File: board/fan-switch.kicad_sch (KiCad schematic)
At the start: 23 parts, among them J1 Conn_01x01, Q1 BXT420N03M, U1 LM1117-3.3

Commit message: WIP
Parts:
- removed ?: (no value), symbol Device:D_Schottky_Dual_CommonCathode_AAK_Parallel
- removed ?: (no value), symbol Drake:ESP-PROG
- removed ? (x5): (no value), symbol Device:R
- removed ? (x4): (no value), symbol Device:C
- removed ?: (no value), symbol Drake:ESP-12
- removed C5: 10u, symbol Device:C_Polarized
- removed C6: 10uF, symbol Device:C_Polarized
- added C1: 10u, Capacitor_SMD:C_0805_2012Metric_Pad1.18x1.45mm_HandSolder, symbol Device:C
- added C2, C3: 47u, Capacitor_SMD:C_0805_2012Metric_Pad1.18x1.45mm_HandSolder, symbol Device:C
- added D1: LED, LED_SMD:LED_0805_2012Metric_Pad1.15x1.40mm_HandSolder, symbol Device:LED
- added J2: PROG, Connector_PinHeader_2.54mm:PinHeader_1x03_P2.54mm_Vertical, symbol Connector:Conn_01x03_Female
- added R1: 270R, Resistor_SMD:R_0805_2012Metric_Pad1.20x1.40mm_HandSolder, symbol Device:R
- added U2: ESP32-C3-WROOM-02, Espressif:ESP32-C3-WROOM-02, symbol Espressif:ESP32-C3-WROOM-02
- D1: renamed from U; value (none) -> SK22; footprint (none) -> Diode_SMD:D_SMB_Handsoldering
- J1: value Conn_01x01 -> 12V; footprint (none) -> Connector_Wire:SolderWire-1sqmm_1x01_D1.4mm_OD3.9mm
- J2: renamed from J1; value Conn_01x01 -> GND; footprint (none) -> Connector_Wire:SolderWire-1sqmm_1x01_D1.4mm_OD3.9mm
- J3: renamed from J1; value Conn_01x01 -> M+; footprint (none) -> Connector_Wire:SolderWire-1sqmm_1x01_D1.4mm_OD3.9mm
- J4: renamed from J1; value Conn_01x01 -> M-; footprint (none) -> Connector_Wire:SolderWire-1sqmm_1x01_D1.4mm_OD3.9mm
- Q1: footprint Package_TO_SOT_SMD:SOT-23_Handsoldering -> Package_TO_SOT_SMD:SOT-23
- R1: renamed from ?; value (none) -> 100; footprint (none) -> Resistor_SMD:R_0805_2012Metric_Pad1.20x1.40mm_HandSolder
- R2: renamed from ?; value (none) -> 10k; footprint (none) -> Resistor_SMD:R_0805_2012Metric_Pad1.20x1.40mm_HandSolder
- U1: footprint (none) -> Package_TO_SOT_SMD:SOT-223-3_TabPin2
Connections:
- net +12V: now also C1.1
- net GATE: now also U2.15 (GPIO3/ADC1_CH3)
- net GND: now also C1.2, C2.2, C3.2, D1.1 (K), J2.2 (Pin_2), U2.19 (GND), U2.9 (GND)
- net 3V3-LOCAL renamed +3V3
- net +3V3: now also C2.1, C3.1, U2.1 (3V3), U2.2 (EN/CHIP_PU)
- new net: D1.2 (A), R1.2
- new net LED: R1.1, U2.3 (GPIO4/ADC1_CH4)
- new net USB_D+: J2.1 (Pin_1), U2.14 (GPIO19/USB_D+)
- new net USB_D-: J2.3 (Pin_3), U2.13 (GPIO18/USB_D-)
- no-connect marks 6 -> 11
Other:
- moved on the sheet: D1, J1, J2, J3, J4, Q1

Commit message: 2.1
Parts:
- removed J2: PROG, Connector_PinHeader_2.54mm:PinHeader_1x03_P2.54mm_Vertical, symbol Connector:Conn_01x03_Female
- removed U1: LM1117-3.3, Package_TO_SOT_SMD:SOT-223-3_TabPin2, symbol Regulator_Linear:LM1117-3.3
- removed U2: ESP32-C3-WROOM-02, Espressif:ESP32-C3-WROOM-02, symbol Espressif:ESP32-C3-WROOM-02
- added A1: 31mm, Drake:Wire antena 2.4GHz, symbol Device:Antenna
- added C4: 10u, Capacitor_SMD:C_0805_2012Metric, symbol Device:C
- added C5, C6: 100n, Capacitor_SMD:C_0805_2012Metric, symbol Device:C
- added J3: TX, Connector_PinHeader_2.54mm:PinHeader_1x01_P2.54mm_Vertical, symbol Connector_Generic:Conn_01x01
- added U1: LM1117MP-3.3, Package_TO_SOT_SMD:SOT-223-3_TabPin2, symbol Regulator_Linear:LM1117MP-3.3
- added U2: PAN2110P0AA, Package_SO:SOIC-8_3.9x4.9mm_P1.27mm, symbol Drake:PAN2110P0AA
- added U3: PY32F003W1xSx, Package_SO:SOIC-16_3.9x9.9mm_P1.27mm, symbol MCU_Puya_PY32F:PY32F003W1xSx
- added X1: SWD, Drake:SWD, symbol Drake:SWD
- added Y1: 16MHz, Crystal:Crystal_SMD_3225-4Pin_3.2x2.5mm, symbol Device:Crystal_GND24_Small
- C1: footprint Capacitor_SMD:C_0805_2012Metric_Pad1.18x1.45mm_HandSolder -> Capacitor_SMD:C_0805_2012Metric
- C2: value 47u -> 1u; footprint Capacitor_SMD:C_0805_2012Metric_Pad1.18x1.45mm_HandSolder -> Capacitor_SMD:C_0805_2012Metric
- C3: value 47u -> 100n; footprint Capacitor_SMD:C_0805_2012Metric_Pad1.18x1.45mm_HandSolder -> Capacitor_SMD:C_0805_2012Metric
- Q1: value BXT420N03M -> AO3400A
- R3: renamed from R1; value 270R -> 330R
- renumbered D1 to D2, J3 to J4, J4 to J5, R2 to R1, R1 to R2
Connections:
- net +12V: now also U1.3 (VI)
- net +3V3: now also C4.1, C5.1, U1.2 (VO), U2.4 (VDD), U3.1 (VSS)
- net GATE: now also U3.15 (PB1)
- net GND: now also C4.2, C5.2, C6.2, U1.1 (GND), U2.7 (VSS), U3.16 (VCC), X1.2 (GND), Y1.2 (G), Y1.4 (G)
- net LED: now also U3.14 (PB0)
- new net: U2.5 (XC1), Y1.1
- new net: U2.6 (XC0), Y1.3
- new net: A1.1 (A), U2.8 (ANT)
- new net: C6.1, U3.5 (PF0/PF2-NRST)
- new net RF_DATA: U2.3 (SDA/DATA), U3.7 (PA1)
- new net RF_SCK: U2.2 (SCL/SCK), U3.8 (PA2)
- new net SWCLK: U3.4 (PF1/PA14-SWC), X1.3 (SWCLK)
- new net SWDIO: U3.3 (PA13-SWD), X1.1 (SWDIO)
- new net TX: J3.1 (Pin_1), U3.13 (PA7)
- new net ~{RF_CS}: U2.1 (CSN), U3.10 (PA4)
- no-connect marks 11 -> 5

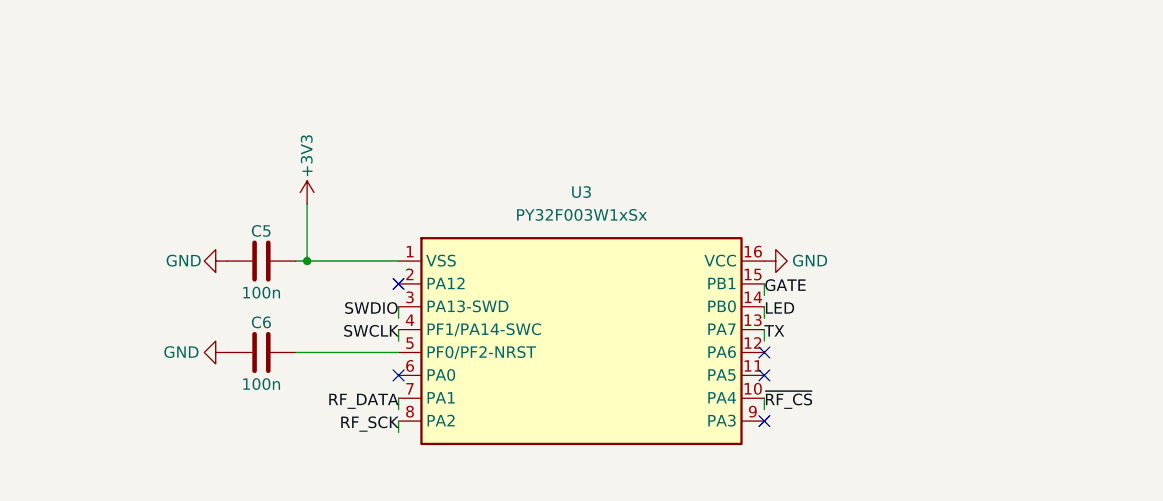
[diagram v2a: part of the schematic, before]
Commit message: Refactor fan control and update schematic
- Updated fan PWM configuration in main.go to use TIM14 on PB1 with a frequency of 50 kHz.
- Added setupFanPWM and setFanDuty methods to manage fan speed via PWM.
- Adjusted pin assignments for SPI communication.
- Modified the schematic to reflect new pin locations and updated component positions.
- Changed Makefile to include new commands for project management.
- Updated test-hub.go with new UID and Key values for the fan device.
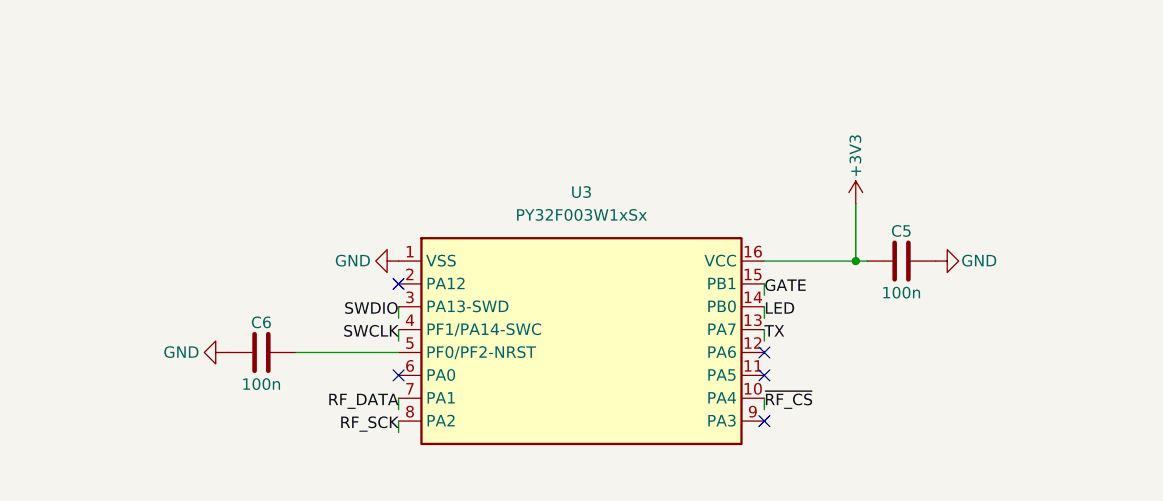
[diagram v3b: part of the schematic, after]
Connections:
- net +3V3: now also U3.16 (VCC); no longer U3.1 (VSS)
- net GND: now also U3.1 (VSS); no longer U3.16 (VCC)
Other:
- moved on the sheet: C5
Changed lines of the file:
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@@
 	)
 	(junction
-		(at 121.92 49.53)
+		(at 182.88 49.53)
 		(diameter 0)
 		(color 0 0 0 0)
@@
 	(wire
 		(pts
-			(xy 121.92 43.18) (xy 121.92 49.53)
+			(xy 182.88 43.18) (xy 182.88 49.53)
 		)
 		(stroke
@@
 	(wire
 		(pts
-			(xy 121.92 49.53) (xy 132.08 49.53)
+			(xy 182.88 49.53) (xy 172.72 49.53)
 		)
 		(stroke
@@
 	(wire
 		(pts
-			(xy 120.65 49.53) (xy 121.92 49.53)
+			(xy 184.15 49.53) (xy 182.88 49.53)
 		)
 		(stroke
@@
 	(symbol
 		(lib_id "power:GND")
-		(at 113.03 49.53 270)
+		(at 191.77 49.53 90)
+		(mirror x)
 		(unit 1)
 		(exclude_from_sim no)
@@
 		(dnp no)
 		(property "Reference" "#PWR013"
-			(at 106.68 49.53 0)
+			(at 198.12 49.53 0)
 			(effects
 				(font
@@
 		)
 		(property "Value" "GND"
-			(at 108.204 49.53 90)
+			(at 196.596 49.53 90)
 			(effects
 				(font
@@
 		)
 		(property "Footprint" ""
-			(at 113.03 49.53 0)
+			(at 191.77 49.53 0)
 			(effects
 				(font
@@
 		)
 		(property "Datasheet" ""
-			(at 113.03 49.53 0)
+			(at 191.77 49.53 0)
 			(effects
 				(font
@@
 		)
 		(property "Description" "Power symbol creates a global label with name \"GND\" , ground"
-			(at 113.03 49.53 0)
+			(at 191.77 49.53 0)
 			(effects
 				(font
@@
 	(symbol
 		(lib_id "power:+3.3V")
-		(at 121.92 43.18 0)
+		(at 182.88 43.18 0)
+		(mirror y)
 		(unit 1)
 		(exclude_from_sim no)
@@
 		(dnp no)
 		(property "Reference" "#PWR015"
-			(at 121.92 46.99 0)
+			(at 182.88 46.99 0)
 			(effects
 				(font
@@
 		)
 		(property "Value" "+3V3"
-			(at 121.92 37.846 90)
+			(at 182.88 37.846 90)
 			(effects
 				(font
@@
 		)
 		(property "Footprint" ""
-			(at 121.92 43.18 0)
+			(at 182.88 43.18 0)
 			(effects
 				(font
@@
 		)
 		(property "Datasheet" ""
-			(at 121.92 43.18 0)
+			(at 182.88 43.18 0)
 			(effects
 				(font
@@
 		)
 		(property "Description" "Power symbol creates a global label with name \"+3.3V\""
-			(at 121.92 43.18 0)
+			(at 182.88 43.18 0)
 			(effects
 				(font
@@
 	(symbol
 		(lib_id "Device:C")
-		(at 116.84 49.53 270)
+		(at 187.96 49.53 90)
+		(mirror x)
 		(unit 1)
 		(exclude_from_sim no)
@@
 		(dnp no)
 		(property "Reference" "C5"
-			(at 116.84 46.228 90)
+			(at 187.96 46.228 90)
 			(effects
 				(font
@@
 		)
 		(property "Value" "100n"
-			(at 116.84 53.086 90)
+			(at 187.96 53.086 90)
 			(effects
 				(font
@@
 		)
 		(property "Footprint" "Capacitor_SMD:C_0805_2012Metric"
-			(at 113.03 50.4952 0)
+			(at 191.77 50.4952 0)
 			(effects
 				(font
@@
 		)
 		(property "Datasheet" "~"
-			(at 116.84 49.53 0)
+			(at 187.96 49.53 0)
 			(effects
 				(font
@@
 		)
 		(property "Description" "Unpolarized capacitor"
-			(at 116.84 49.53 0)
+			(at 187.96 49.53 0)
 			(effects
 				(font
@@
 	(symbol
 		(lib_id "power:GND")
-		(at 172.72 49.53 90)
+		(at 132.08 49.53 270)
 		(mirror x)
 		(unit 1)
@@
 		(dnp no)
 		(property "Reference" "#PWR016"
-			(at 179.07 49.53 0)
+			(at 125.73 49.53 0)
 			(effects
 				(font
@@
 		)
 		(property "Value" "GND"
-			(at 177.8 49.53 90)
+			(at 127 49.53 90)
 			(effects
 				(font
@@
 		)
 		(property "Footprint" ""
-			(at 172.72 49.53 0)
+			(at 132.08 49.53 0)
 			(effects
 				(font
@@
 		)
 		(property "Datasheet" ""
-			(at 172.72 49.53 0)
+			(at 132.08 49.53 0)
 			(effects
 				(font
@@
 		)
 		(property "Description" "Power symbol creates a global label with name \"GND\" , ground"
-			(at 172.72 49.53 0)
+			(at 132.08 49.53 0)
 			(effects
 				(font
